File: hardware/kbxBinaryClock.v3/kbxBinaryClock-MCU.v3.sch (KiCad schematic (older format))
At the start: 56 parts, among them J1 GS3, P1 STM32_SWD_USART, Q1 2N7002, Q2 2N7002, Q3 2N7002, Q4 2N7002, Q5 Q_Photo_NPN, SW1 SW_Push, U1 STM32F072CBTx, Y1 32.768 KHz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

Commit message: Modified PCBs to accommodate a 16mm buzzer element
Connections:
- net GND: now also RV1.3
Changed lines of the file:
@@
 Connection ~ 4350 1400
 Wire Wire Line
-	4600 1400 4350 1400
+	4200 1400 4600 1400
 Wire Wire Line
 	4350 1250 4350 1450
@@
 	1    0    0    -1
 $EndComp
+Wire Wire Line
+	4200 1100 4200 1400
 $EndSCHEMATC

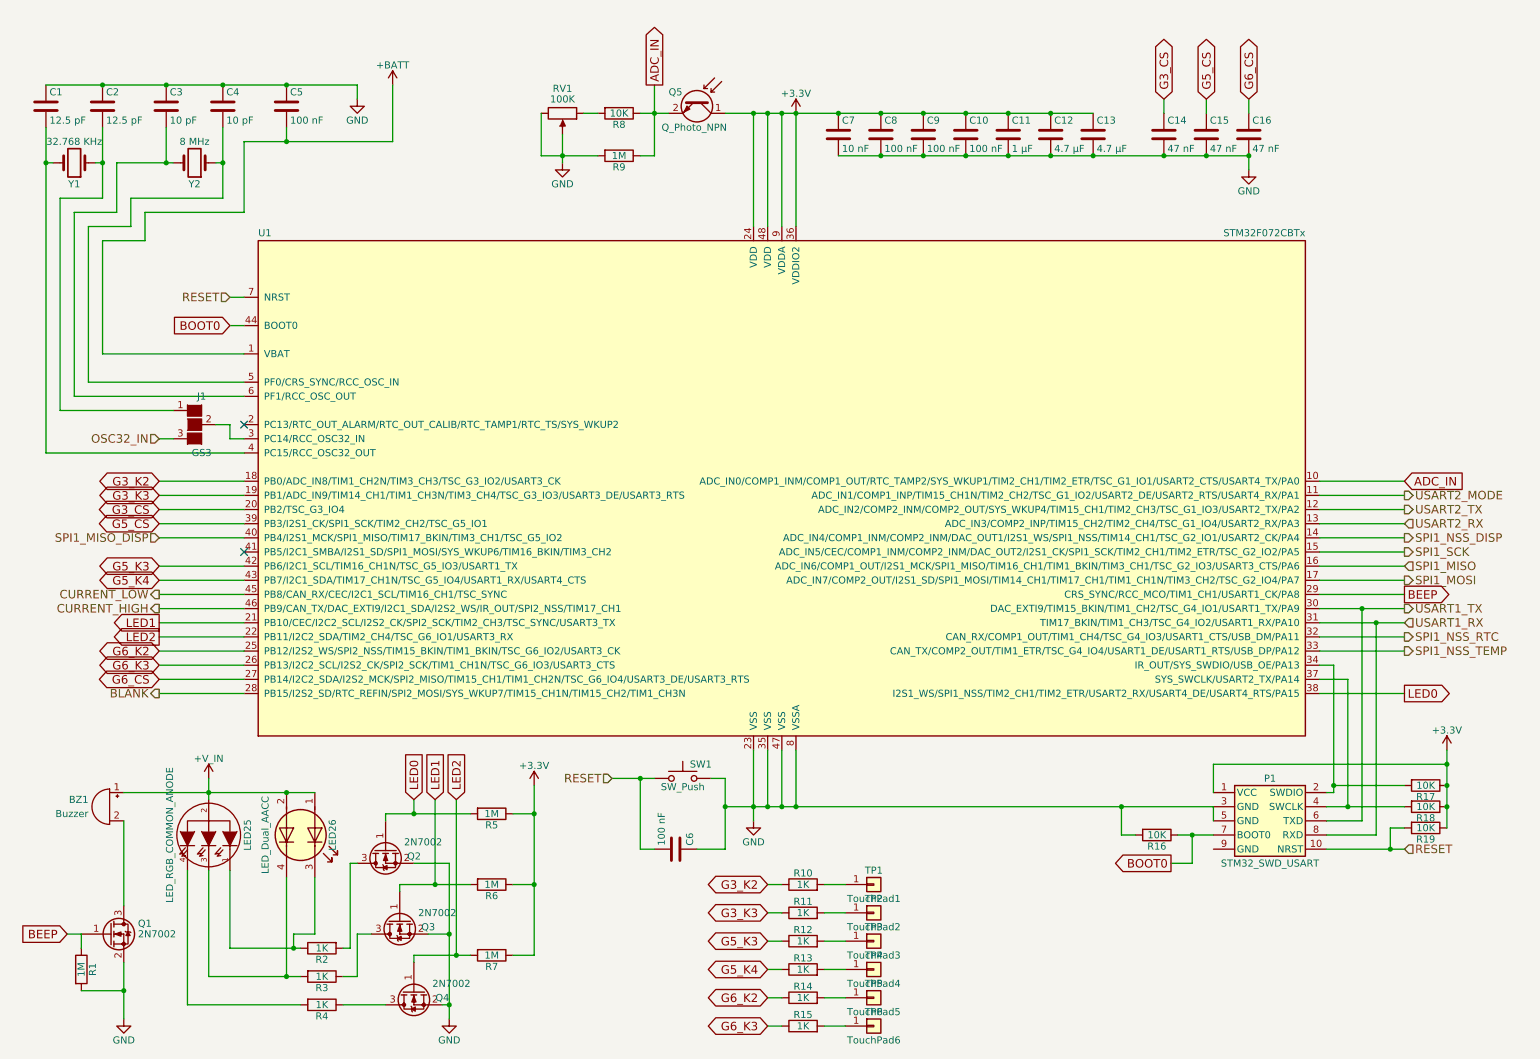
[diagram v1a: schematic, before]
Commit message: Added BoM, hw README, PCB tweaks
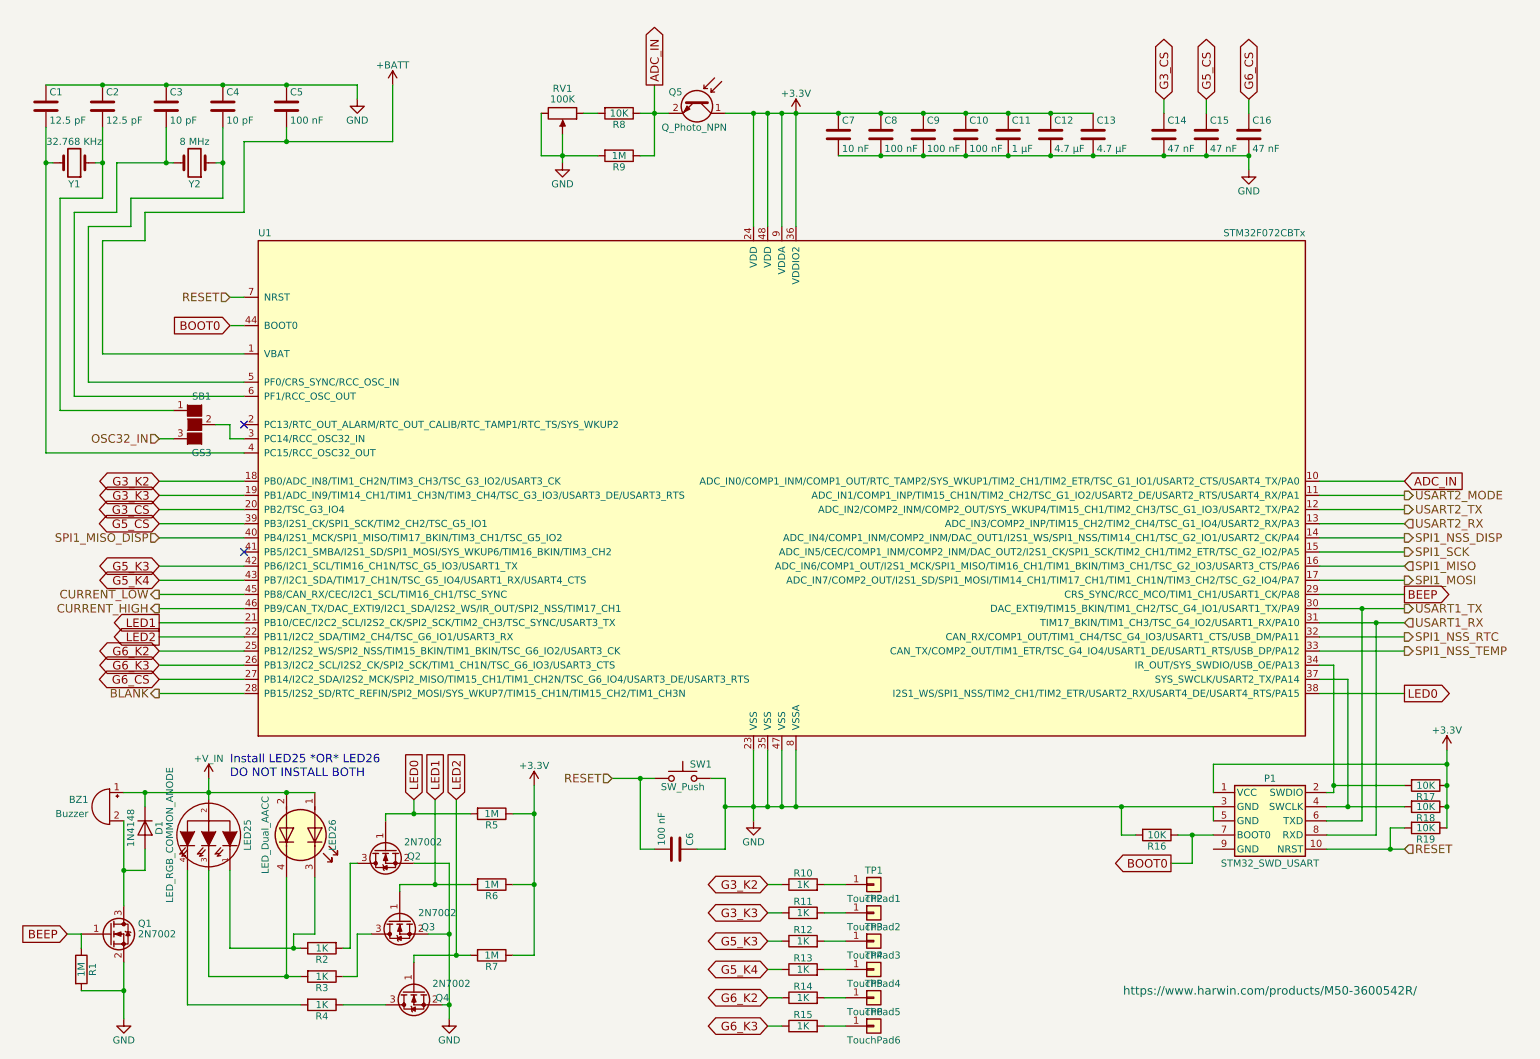
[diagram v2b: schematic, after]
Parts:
- added D1: 1N4148, Diodes_SMD:D_SOD-123, symbol D
- BZ1: Part Number (none) -> TDK SD1614TT-B1
- LED26: Part Number (none) -> CMD1522SRUGCTR8
- P1: Part Number (none) -> M50-3600542R
- Q5: Part Number (none) -> TEPT5600
- RV1: Part Number (none) -> TC33X-2-104E
- SW1: Part Number (none) -> KMR221G LFS
- Y1: Part Number (none) -> ECX-.327-CDX-1293
- Y2: Part Number (none) -> ABM3B-8.000MHZ-10-1UT
- renumbered J1 to SB1
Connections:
- net +V_IN: now also D1.1 (K)
- net at BZ1.2 (+), Q1.3 (D): now also D1.2 (A)
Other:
- note added: "Install LED25 *OR* LED26\nDO NOT INSTALL BOTH"
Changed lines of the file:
@@
 F 1 "SW_Push" H 5200 5740 50  0000 C CNN
 F 2 "Buttons_Switches_SMD:SW_SPST_KMR2" H 5200 6000 50  0001 C CNN
-F 3 "" H 5200 6000 50  0001 C CNN
+F 3 "https://www.ckswitches.com/media/1479/kmr2.pdf" H 5200 6000 50  0001 C CNN
+F 4 "KMR221G LFS" H 5200 5800 60  0001 C CNN "Part Number"
 	1    5200 5800
 	1    0    0    -1
@@
 F 1 "8 MHz" H 1750 1300 50  0000 C CNN
 F 2 "Crystals:Crystal_SMD_5032-4pin_5.0x3.2mm" H 1750 1450 50  0001 C CNN
-F 3 "" H 1750 1450 50  0001 C CNN
+F 3 "http://www.abracon.com/Resonators/abm3b.pdf" H 1750 1450 50  0001 C CNN
+F 4 "ABM3B-8.000MHZ-10-1UT" H 1750 1450 60  0001 C CNN "Part Number"
 	1    1750 1450
 	-1   0    0    1
@@
 F 1 "LED_Dual_AACC" H 2500 5950 50  0000 C CNN
 F 2 "LEDs:LED_Cree-PLCC4_3.2x2.8mm_CCW" H 2530 6200 50  0001 C CNN
-F 3 "" H 2530 6200 50  0001 C CNN
+F 3 "https://www.vcclite.com/product/led-smt-1206-1-72-1v-20ma-redgreen-2k/" H 2530 6200 50  0001 C CNN
+F 4 "CMD1522SRUGCTR8" H 2500 6200 60  0001 C CNN "Part Number"
 	1    2500 6200
 	0    1    1    0
@@
 F 1 "2N7002" V 3150 6400 50  0000 L CNN
 F 2 "TO_SOT_Packages_SMD:SOT-23" H 3400 6725 50  0001 L CIN
-F 3 "" H 3200 6800 50  0001 L CNN
+F 3 "https://www.diodes.com/assets/Datasheets/ds11303.pdf" H 3200 6800 50  0001 L CNN
 	1    3200 6800
 	0    -1   1    0
@@
 F 1 "2N7002" V 3050 5900 50  0000 L CNN
 F 2 "TO_SOT_Packages_SMD:SOT-23" H 3300 6225 50  0001 L CIN
-F 3 "" H 3100 6300 50  0001 L CNN
+F 3 "https://www.diodes.com/assets/Datasheets/ds11303.pdf" H 3100 6300 50  0001 L CNN
 	1    3100 6300
 	0    -1   1    0
@@
 F 1 "Q_Photo_NPN" V 5500 750 50  0000 L CNN
 F 2 "LEDs:LED_D5.0mm" H 5500 1100 50  0001 C CNN
-F 3 "" H 5300 1000 50  0001 C CNN
+F 3 "https://www.vishay.com/docs/84768/tept5600.pdf" H 5300 1000 50  0001 C CNN
+F 4 "TEPT5600" V 5300 1000 60  0001 C CNN "Part Number"
 	1    5300 1000
 	0    1    1    0
@@
 F 1 "Buzzer" H 1300 5950 50  0000 L CNN
 F 2 "Buzzers_Beepers:Buzzer_12x9.5RM7.6" V 1125 6100 50  0001 C CNN
-F 3 "" V 1125 6100 50  0001 C CNN
+F 3 "https://product.tdk.com/en/search/sw_piezo/sw_piezo/em-buzzer/info?part_no=SD1614TT-B1" V 1125 6100 50  0001 C CNN
+F 4 "TDK SD1614TT-B1" H 1150 6000 60  0001 C CNN "Part Number"
 	1    1150 6000
 	-1   0    0    -1
@@
 F 1 "2N7002" H 1350 6900 50  0000 L CNN
 F 2 "TO_SOT_Packages_SMD:SOT-23" H 1350 6825 50  0001 L CIN
-F 3 "" H 1150 6900 50  0001 L CNN
+F 3 "https://www.diodes.com/assets/Datasheets/ds11303.pdf" H 1150 6900 50  0001 L CNN
 	1    1150 6900
 	1    0    0    -1
@@
 F 1 "STM32_SWD_USART" H 9350 5800 50  0000 C CNN
 F 2 "Pin_Headers:Pin_Header_Straight_2x05_Pitch1.27mm_SMD" H 9350 4900 60  0001 C CNN
-F 3 "" H 9350 4900 60  0000 C CNN
+F 3 "https://www.harwin.com/products/M50-3600542R/" H 9350 4900 60  0000 C CNN
+F 4 "M50-3600542R" H 9350 6100 60  0001 C CNN "Part Number"
 	1    9350 6100
 	1    0    0    -1
@@
 F 1 "32.768 KHz" H 900 1300 50  0000 C CNN
 F 2 "Crystals:Crystal_SMD_3215-2pin_3.2x1.5mm" H 900 1450 50  0001 C CNN
-F 3 "" H 900 1450 50  0001 C CNN
+F 3 "https://www.ecsxtal.com/store/pdf/ECX-.327-CDX-1293.pdf" H 900 1450 50  0001 C CNN
+F 4 "ECX-.327-CDX-1293" H 900 1450 60  0001 C CNN "Part Number"
 	1    900  1450
 	-1   0    0    1
@@
 F 1 "100K" V 4250 1100 50  0000 C CNN
 F 2 "Potentiometers:Potentiometer_Trimmer_Vishay_TS53YJ" H 4350 1100 50  0001 C CNN
-F 3 "" H 4350 1100 50  0001 C CNN
+F 3 "http://www.bourns.com/docs/Product-Datasheets/TC33.PDF" H 4350 1100 50  0001 C CNN
+F 4 "TC33X-2-104E" V 4350 1100 60  0001 C CNN "Part Number"
 	1    4350 1100
 	0    1    1    0
@@
 F 1 "2N7002" V 3250 6900 50  0000 L CNN
 F 2 "TO_SOT_Packages_SMD:SOT-23" H 3500 7225 50  0001 L CIN
-F 3 "" H 3300 7300 50  0001 L CNN
+F 3 "https://www.diodes.com/assets/Datasheets/ds11303.pdf" H 3300 7300 50  0001 L CNN
 	1    3300 7300
 	0    -1   1    0
@@
 F 1 "LED_RGB_COMMON_ANODE" H 1850 5925 50  0000 C CNN
 F 2 "LEDs:LED_D5.0mm-4" H 1875 6350 60  0001 C CNN
-F 3 "" H 1875 6350 60  0000 C CNN
+F 3 "https://www.adafruit.com/product/302" H 1875 6350 60  0001 C CNN
 	1    1850 6200
 	0    1    1    0
@@
 Connection ~ 2400 7200
 $Comp
-L GS3 J1
+L GS3 SB1
 U 1 1 5A7D98D2
 P 1750 3300
-F 0 "J1" H 1800 3500 50  0000 C CNN
+F 0 "SB1" H 1800 3500 50  0000 C CNN
 F 1 "GS3" H 1800 3101 50  0000 C CNN
 F 2 "Connectors:GS3" V 1838 3226 50  0001 C CNN
@@
 F 1 "STM32F072CBTx" H 9600 5625 50  0000 R BNN
 F 2 "Housings_QFP:LQFP-48_7x7mm_Pitch0.5mm" H 9600 5575 50  0001 R TNN
-F 3 "" H 5900 3800 50  0001 C CNN
+F 3 "http://www.st.com/content/ccc/resource/technical/document/datasheet/cd/46/43/83/22/d3/40/c8/DM00090510.pdf/files/DM00090510.pdf/jcr:content/translations/en.DM00090510.pdf" H 5900 3800 50  0001 C CNN
 	1    5900 3800
 	1    0    0    -1
@@
 Wire Wire Line
 	4200 1100 4200 1400
+$Comp
+L D D1
+U 1 1 5A8915C5
+P 1400 6150
+F 0 "D1" H 1400 6250 50  0000 C CNN
+F 1 "1N4148" H 1400 6050 50  0000 C CNN
+F 2 "Diodes_SMD:D_SOD-123" H 1400 6150 50  0001 C CNN
+F 3 "https://www.diodes.com/assets/Datasheets/ds30086.pdf" H 1400 6150 50  0001 C CNN
+	1    1400 6150
+	0    1    1    0
+$EndComp
+Wire Wire Line
+	1400 6000 1400 5900
+Connection ~ 1400 5900
+Wire Wire Line
+	1400 6300 1400 6450
+Wire Wire Line
+	1400 6450 1250 6450
+Connection ~ 1250 6450
+Text Notes 2000 5800 0    60   ~ 0
+Install LED25 *OR* LED26\nDO NOT INSTALL BOTH
 $EndSCHEMATC

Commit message: Updated for KiCad v5, updated silks
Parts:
- BZ1: symbol Buzzer -> kbxBinaryClock.v3-rescue:Buzzer
- C1, C10, C11, C12, C13, C14, C15, C16, C2, C3, C4, C5, C6, C7, C8, C9: symbol C -> kbxBinaryClock.v3-rescue:C
- D1: symbol D -> kbxBinaryClock.v3-rescue:D
- LED25: symbol LED_RGB_COMMON_ANODE -> kbxBinaryClock.v3-rescue:LED_RGB_COMMON_ANODE
- LED26: symbol LED_Dual_AACC -> kbxBinaryClock.v3-rescue:LED_Dual_AACC
- P1: symbol STM32_SWD_USART -> kbxBinaryClock.v3-rescue:STM32_SWD_USART
- Q1, Q2, Q3, Q4: symbol 2N7002 -> kbxBinaryClock.v3-rescue:2N7002
- Q5: symbol Q_Photo_NPN -> kbxBinaryClock.v3-rescue:Q_Photo_NPN
- R1, R10, R11, R12, R13, R14, R15, R16, R17, R18, R19, R2, R3, R4, R5, R6, R7, R8, R9: symbol R -> kbxBinaryClock.v3-rescue:R
- RV1: symbol POT -> kbxBinaryClock.v3-rescue:POT
- SB1: symbol GS3 -> kbxBinaryClock.v3-rescue:GS3
- SW1: symbol SW_Push -> kbxBinaryClock.v3-rescue:SW_Push
- TP1, TP2, TP3, TP4, TP5, TP6: symbol Conn_01x01 -> kbxBinaryClock.v3-rescue:Conn_01x01
- U1: symbol STM32F072CBTx -> kbxBinaryClock.v3-rescue:STM32F072CBTx
- Y1, Y2: symbol Crystal -> kbxBinaryClock.v3-rescue:Crystal
